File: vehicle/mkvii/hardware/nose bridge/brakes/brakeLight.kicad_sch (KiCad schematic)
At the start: 25 parts, among them Q5 Q_NMOS_SSM3K333R, U2 U_OPAMP_MCP6001, U3 U_OPAMP_MCP6001, U8 U_GATE_SN74LVC1G32DBVR

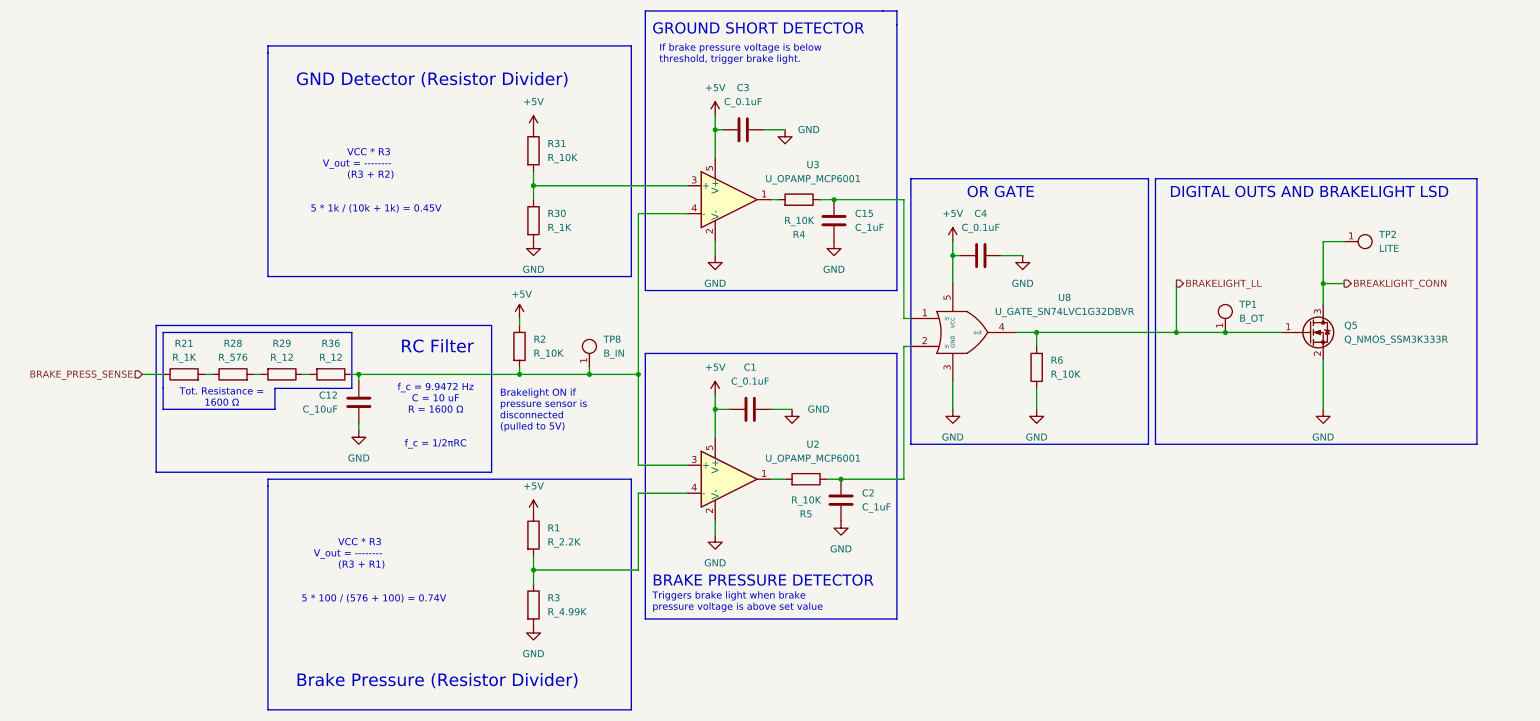
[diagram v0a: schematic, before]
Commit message: BSPD Schmatics Update v2 (with 10-22-2024 revisions from Ian Walsh)
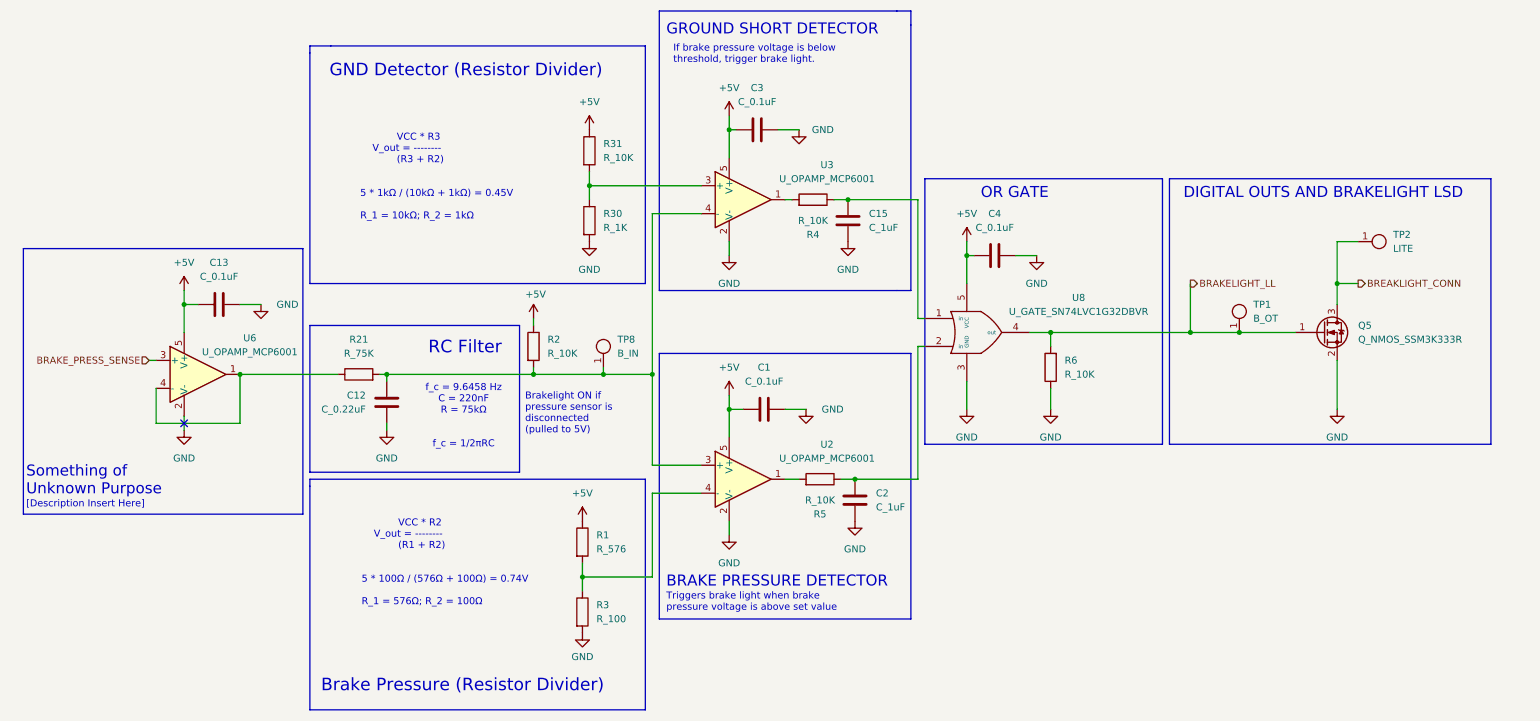
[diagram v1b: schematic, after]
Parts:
- removed C12: C_10uF, OEM:C_0603, symbol OEM:C_10uF
- removed R1: R_2.2K, OEM:R_0603, symbol OEM:R_2.2K
- removed R21: R_1K, OEM:R_0603, symbol OEM:R_1K
- removed R28: R_576, OEM:R_0603, symbol OEM:R_576
- removed R29, R36: R_12, OEM:R_0603, symbol OEM:R_12
- removed R3: R_4.99K, OEM:R_0603, symbol OEM:R_4.99K
- added C12: C_0.22uF, OEM:C_0603, symbol OEM:C_0.22uF
- added C13: C_0.1uF, OEM:C_0603, symbol OEM:C_0.1uF
- added R1: R_576, OEM:R_0603, symbol OEM:R_576
- added R21: R_75K, OEM:R_0603, symbol OEM:R_75K
- added R3: R_100, OEM:R_0603, symbol OEM:R_100
- added U6: U_OPAMP_MCP6001, Package_TO_SOT_SMD:SOT-353_SC-70-5, symbol OEM:U_OPAMP_MCP6001
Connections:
- net +5V: now also C13.1, R1.1, U6.5 (V+)
- net BRAKE_PRESS_SENSE: now also U6.3 (+)
- net GND: now also C12.2, C13.2, R3.2, U6.2 (V-)
- net at R2.2, TP8.1, U2.3 (+)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: now also C12.1, R21.2
- net at U2.4 (-): now also R1.2, R3.1
- new net: R21.1, U6.1, U6.4 (-)
- no-connect marks 0 -> 1
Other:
- note added: "Something of Unknown Purpose"
- note added: "VCC * R2 V_out = -------- (R1 + R2) 5 * 100Ω / (576Ω + 100Ω) = 0.74V R_1 = 576Ω; R_2 = 100Ω"
- note added: "VCC * R3 V_out = -------- (R3 + R2) 5 * 1kΩ / (10kΩ + 1kΩ) = 0.45V R_1 = 10kΩ; R_2 = 1kΩ"
- note added: "[Description Insert Here]"
- note added: "f_c = 9.6458 Hz C = 220nF R = 75kΩ f_c = 1/2πRC"
- note removed: "Tot. Resistance = 1600 Ω"
- note removed: "VCC * R3 V_out = -------- (R3 + R1) 5 * 100 / (576 + 100) = 0.74V"
- note removed: "VCC * R3 V_out = -------- (R3 + R2) 5 * 1k / (10k + 1k) = 0.45V"
- note removed: "f_c = 9.9472 Hz C = 10 uF R = 1600 Ω f_c = 1/2πRC"
- moved on the sheet: C1, C15, C2, C3, C4, Q5, R2, R30, R31, R4, R5, R6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

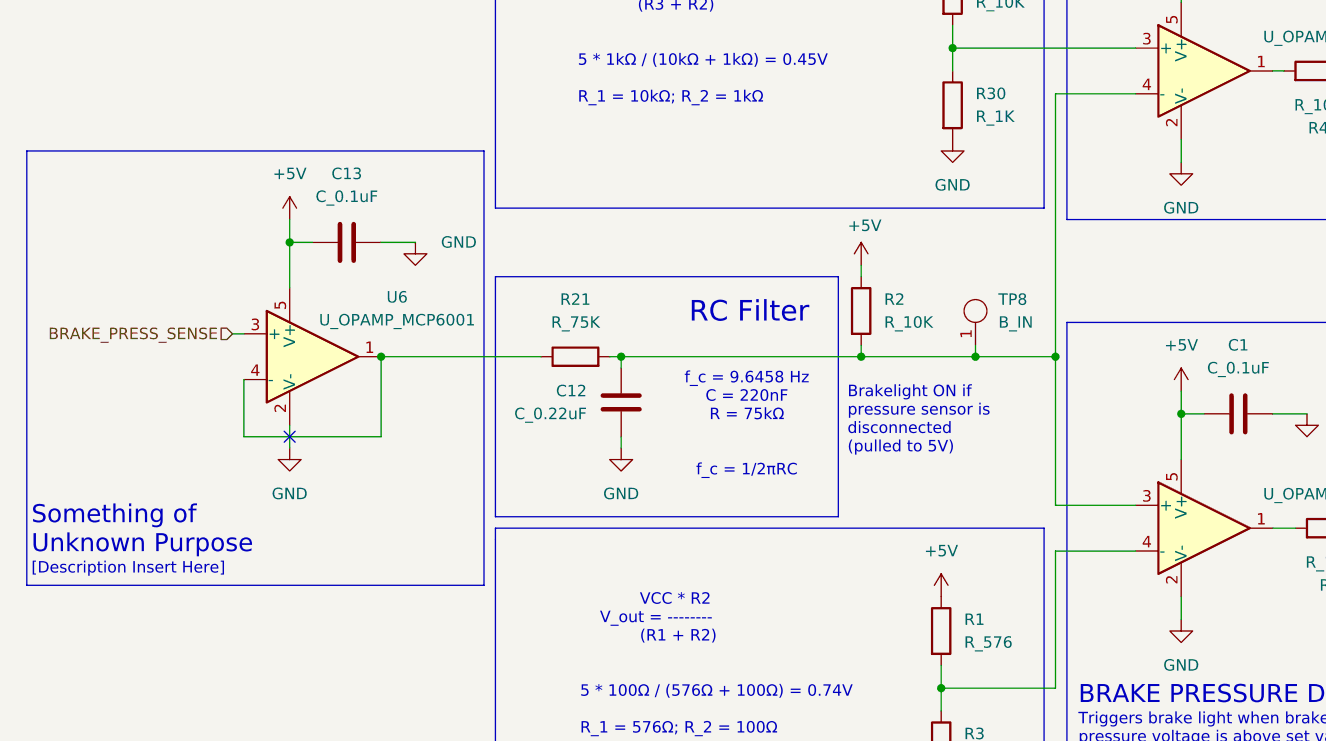
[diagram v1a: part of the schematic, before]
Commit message: BSPD Schematics Update v3 (with added BRAKE_PRESS_SENSE_FILTERED and RC_TIMER_STATUS and relevant connections in top level view and microcontroller pages; moved 5k resistor)
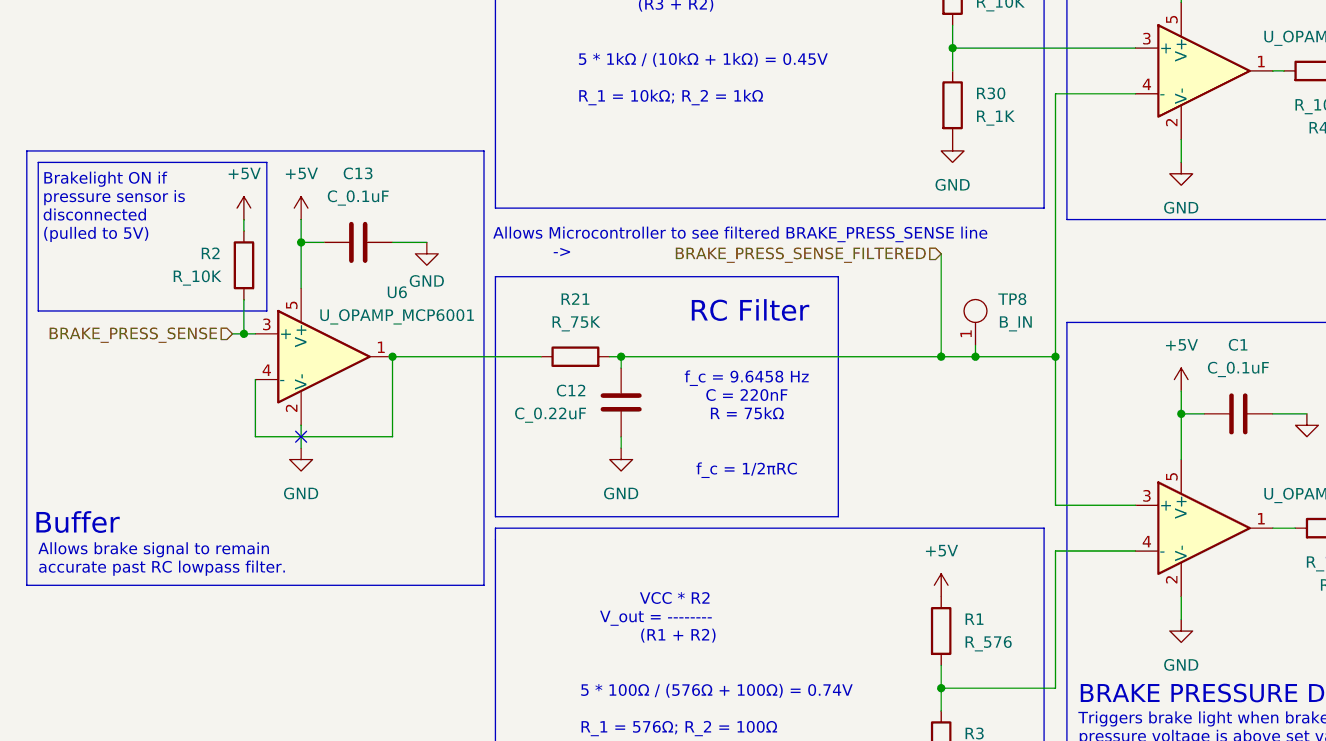
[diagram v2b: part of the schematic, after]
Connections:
- net BRAKE_PRESS_SENSE: now also R2.2
- net BRAKE_PRESS_SENSE_FILTERED: now reaches C12.1, R21.2, TP8.1, U2.3 (+), U3.4 (-)
- net BRAKE_PRESS_SENSE_FILTERED: no longer R2.2
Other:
- note added: "Allows Microcontroller to see filtered BRAKE_PRESS_SENSE line ->"
- note added: "Allows brake signal to remain accurate past RC lowpass filter."
- note added: "Buffer"
- note removed: "Something of Unknown Purpose"
- note removed: "[Description Insert Here]"
- moved on the sheet: C13, U6

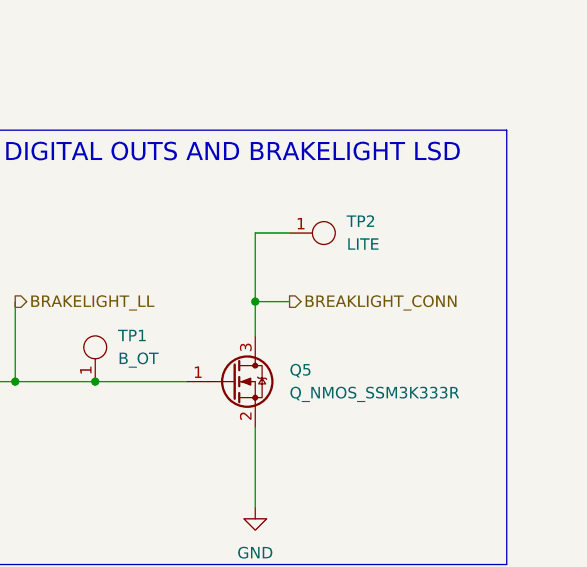
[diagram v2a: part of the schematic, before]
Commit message: BSPD Update - New PCB Layout is complete with this update. Added LED for BSPD_TRIP_LED output from Microcontroller.
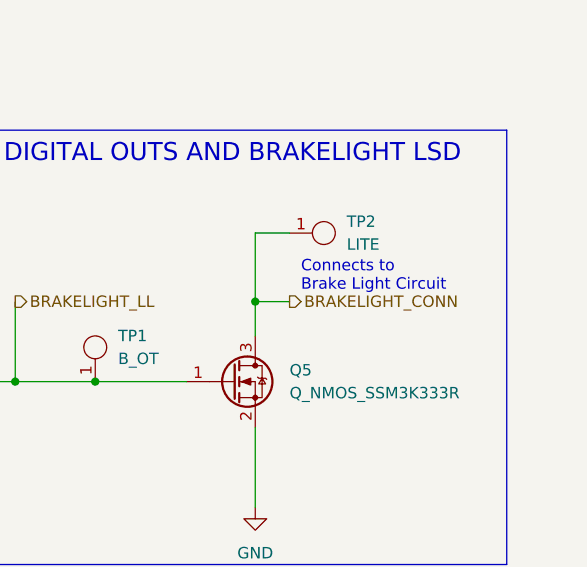
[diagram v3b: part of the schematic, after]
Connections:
- net BREAKLIGHT_CONN renamed BRAKELIGHT_CONN
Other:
- note added: "Connects to Brake Light Circuit"
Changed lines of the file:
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@@
+		)
+	)
+	(text "Connects to \nBrake Light Circuit"
+		(exclude_from_sim no)
+		(at 259.08 86.106 0)
+		(effects
+			(font
+				(size 1.27 1.27)
+			)
+			(justify left)
 		)
 	)
@@
 		)
 	)
-	(hierarchical_label "BREAKLIGHT_CONN"
+	(hierarchical_label "BRAKELIGHT_CONN"
 		(shape output)
 		(at 257.81 88.9 0)
